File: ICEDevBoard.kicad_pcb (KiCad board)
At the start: 4 copper layers, 100 x 100 mm, 233 parts, among them J101 USB4215-03-A_REVA, J301 program, J401 VGA, J501 Joystick, J502 SJ2-35813B-SMT-TR, J503 Keyboard, J504 Mouse, J505 MSD-1-A, J701 PMOD, Q101 BC847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

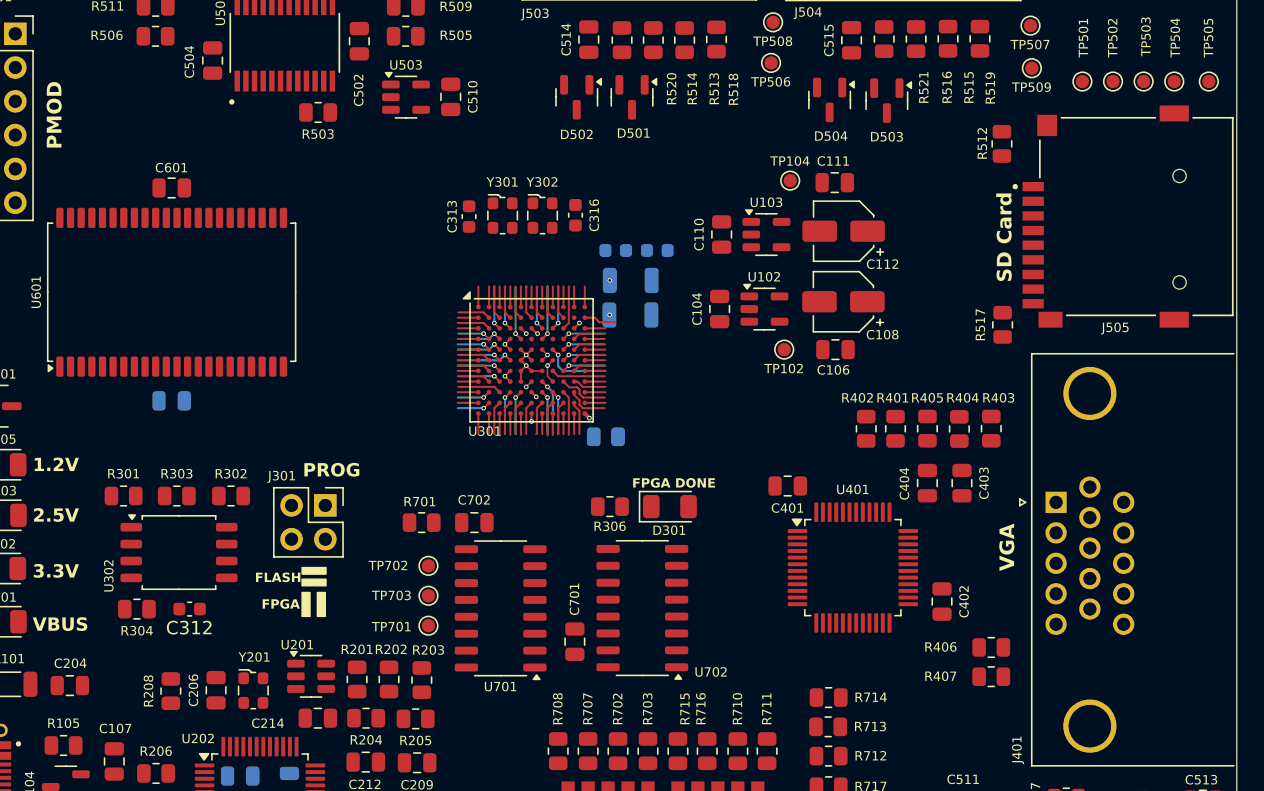
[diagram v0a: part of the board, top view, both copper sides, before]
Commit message: Started board routing
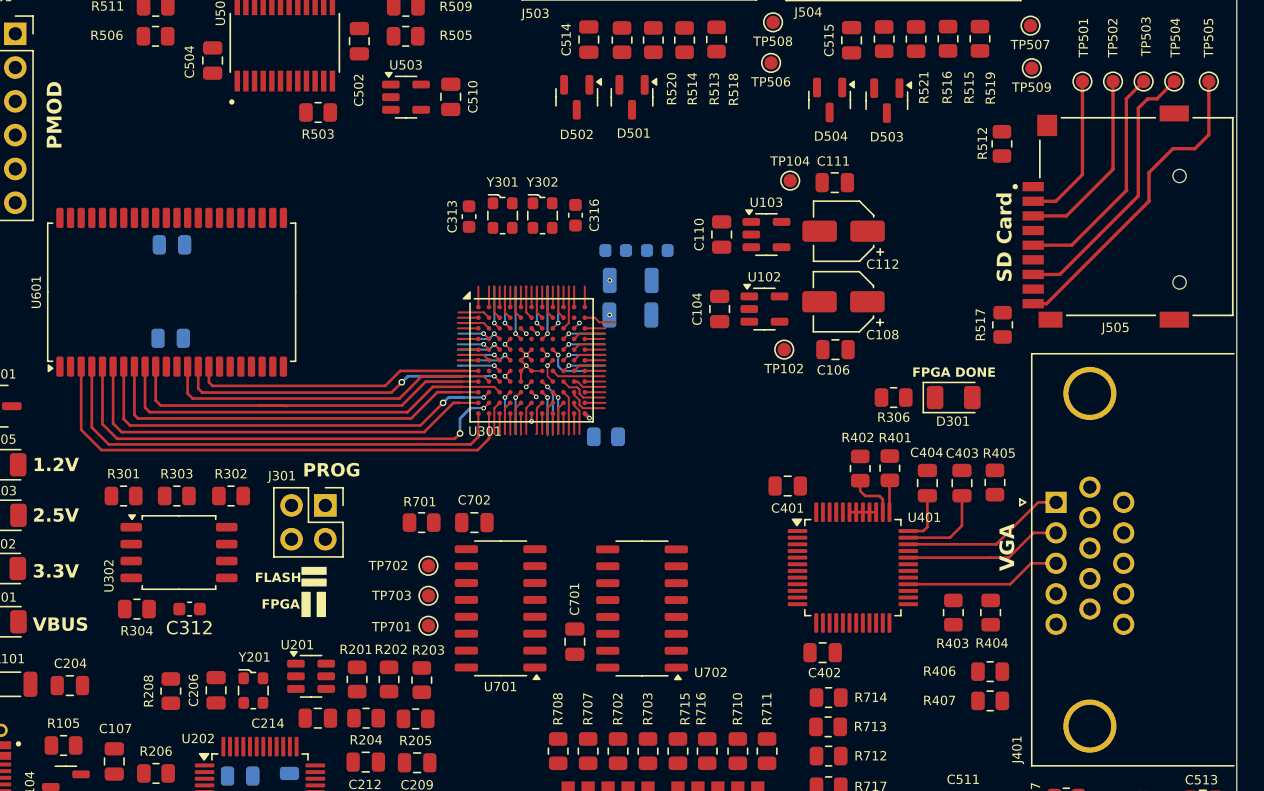
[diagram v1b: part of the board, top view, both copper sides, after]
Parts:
- C601: moved to B.Cu
- moved R306 22.8 mm to (174.2, 93.3)
- moved D301 22.8 mm to (178.7, 93.3)
- moved R403 14.1 mm to (178.7, 109.5), turned to -90 degrees
- moved R404 14.0 mm to (181.5, 109.5), turned to -90 degrees
- moved C402 9.76 mm to (168.9, 112.5), turned to 0 degrees
- moved R405 6.49 mm to (181.8, 99.7)
- moved C602 4.70 mm to (119.9, 88.9)
- moved C601 4.28 mm to (120.0, 81.9)
- moved R402 3.02 mm to (171.7, 98.7), turned to -90 degrees
- moved R401 2.99 mm to (173.9, 98.7), turned to 90 degrees
- moved R406 1.82 mm to (181.5, 114.0)
- moved R407 1.82 mm to (181.5, 116.2)
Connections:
- U301 pad F1: /FPGA/MEM_A7 -> /FPGA/MEM_A6
- U301 pad F2: /FPGA/MEM_A9 -> /FPGA/MEM_A5
- U301 pad G2: /FPGA/MEM_A5 -> /FPGA/MEM_A9
- U301 pad G3: /FPGA/MEM_A6 -> /FPGA/MEM_A7
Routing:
- net /FPGA/MEM_A0: track 1.55 -> 38.5 mm
- net /FPGA/MEM_A1: track 1.55 -> 36.3 mm
- net /FPGA/MEM_A2: track 2.52 -> 35.6 mm, vias 1 -> 2
- net /FPGA/MEM_A3: track 1.55 -> 33.1 mm
- net /FPGA/MEM_A4: track 2.63 -> 33.2 mm, vias 1 -> 2
- net /FPGA/~{SRAM_CE}: track 1.55 -> 30.7 mm
- net /FPGA/MEM_D1: track 1.55 -> 30.0 mm
- net /FPGA/MEM_D0: track 3.27 -> 31.1 mm
- net /FPGA/SD_DETECT: track 3.27 -> 27.0 mm
- net /FPGA/MEM_D2: track 2.52 -> 26.1 mm
- net /FPGA/MEM_D3: track 3.27 -> 25.3 mm, vias 1 -> 2
- net /FPGA/~{SRAM_WE}: track 1.55 -> 22.7 mm
- net /FPGA/SD_MISO: track 2.47 -> 22.9 mm
- net /FPGA/SD_CLOCK: track 1.55 -> 19.0 mm
- net /FPGA/SD_MOSI: track 2.39 -> 16.4 mm
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
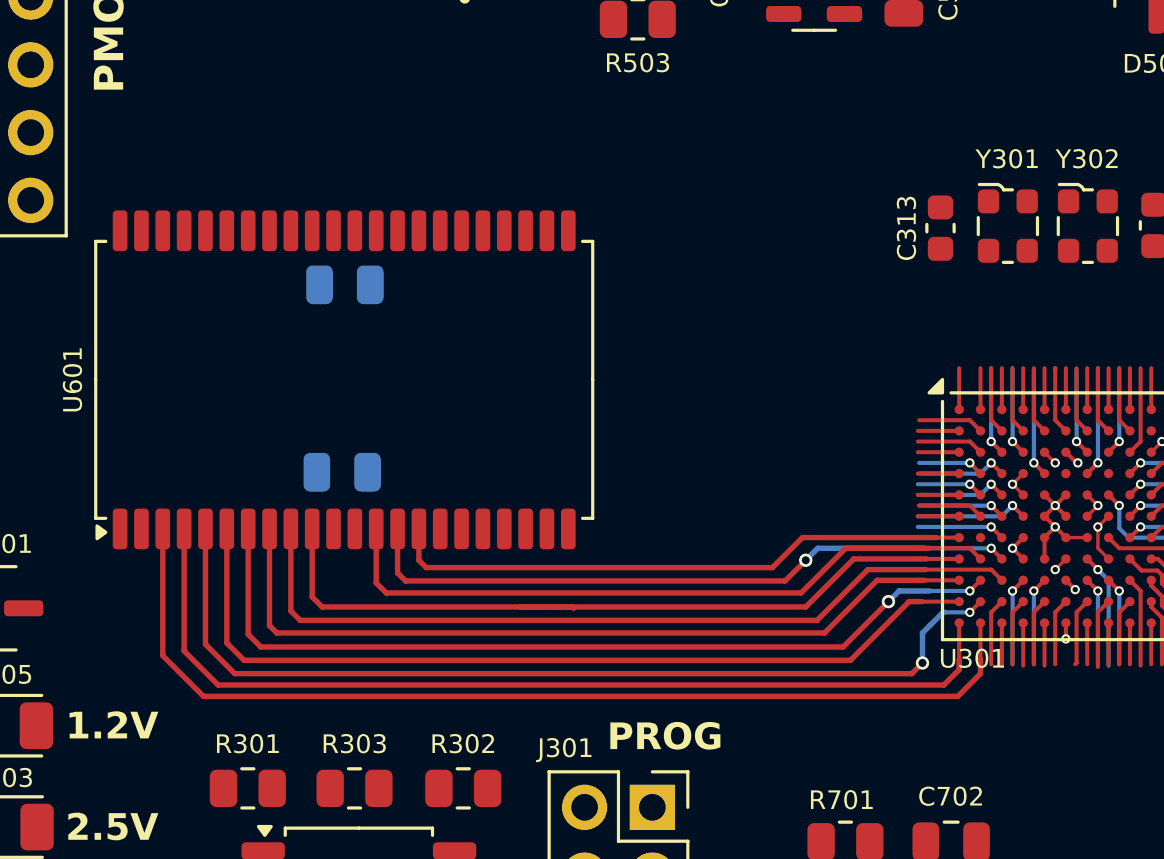
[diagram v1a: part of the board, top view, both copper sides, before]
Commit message: Routed SRAM
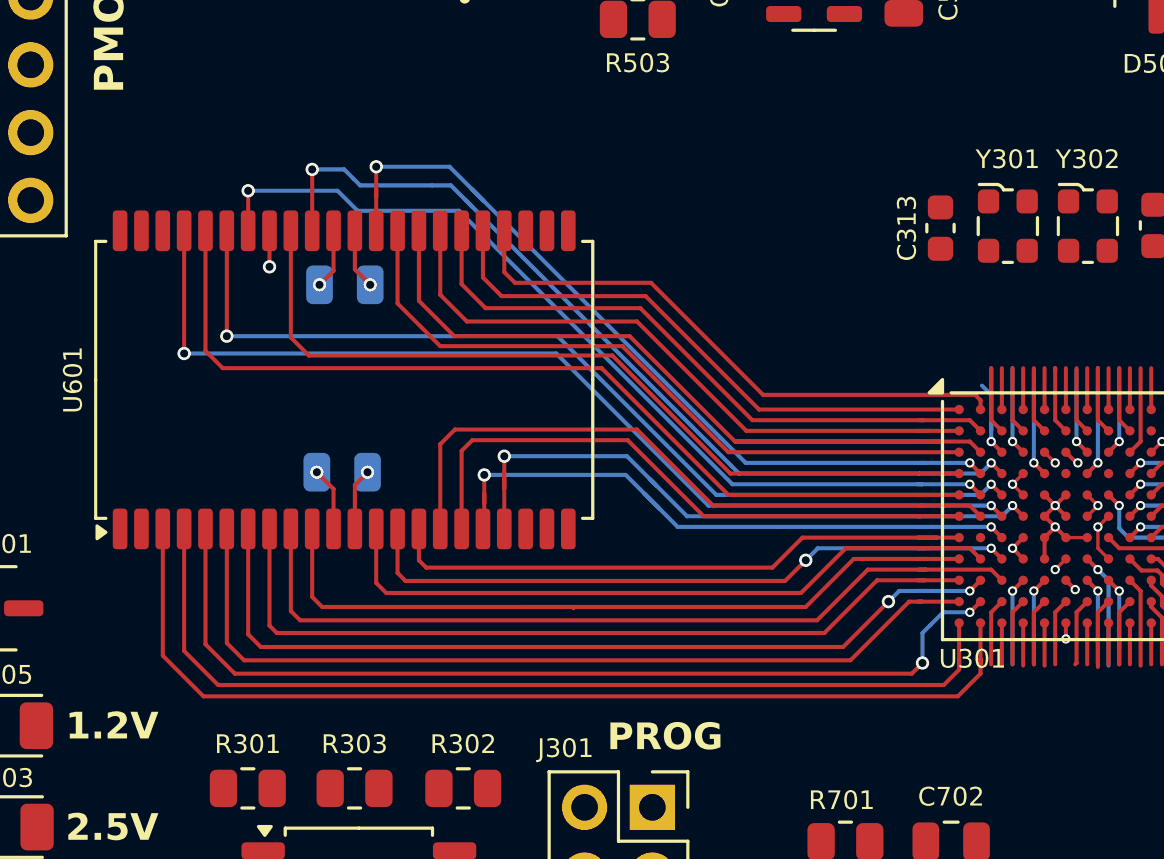
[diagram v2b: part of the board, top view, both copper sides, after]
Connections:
- U301 pad A1: /FPGA/MEM_A10 -> /FPGA/MEM_A11
- U301 pad A2: /FPGA/MEM_A11 -> /FPGA/MEM_A10
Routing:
- net /FPGA/MEM_A18: track 3.27 -> 37.8 mm, vias 1 -> 2
- net /FPGA/MEM_A17: track 1.55 -> 35.1 mm
- net /FPGA/MEM_A16: track 3.48 -> 35.8 mm, vias 1 -> 2
- net /FPGA/MEM_A15: track 2.52 -> 33.8 mm, vias 1 -> 2
- net /FPGA/MEM_A14: track 2.52 -> 33.7 mm
- net /FPGA/MEM_D6: track 3.53 -> 33.7 mm, vias 1 -> 2
- net /FPGA/MEM_D7: track 1.55 -> 31.2 mm
- net /FPGA/MEM_D5: track 2.47 -> 31.0 mm, vias 1 -> 2
- net /FPGA/MEM_D4: track 1.55 -> 26.1 mm
- net /FPGA/MEM_A13: track 1.55 -> 24.4 mm
- net /FPGA/MEM_A5: track 2.47 -> 25.1 mm
- net /FPGA/MEM_A6: track 1.55 -> 23.1 mm
- net /FPGA/MEM_A12: track 2.47 -> 23.9 mm
- net /FPGA/MEM_A8: track 4.28 -> 24.5 mm, vias 1 -> 2
- net /FPGA/MEM_A10: track 1.55 -> 21.7 mm
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
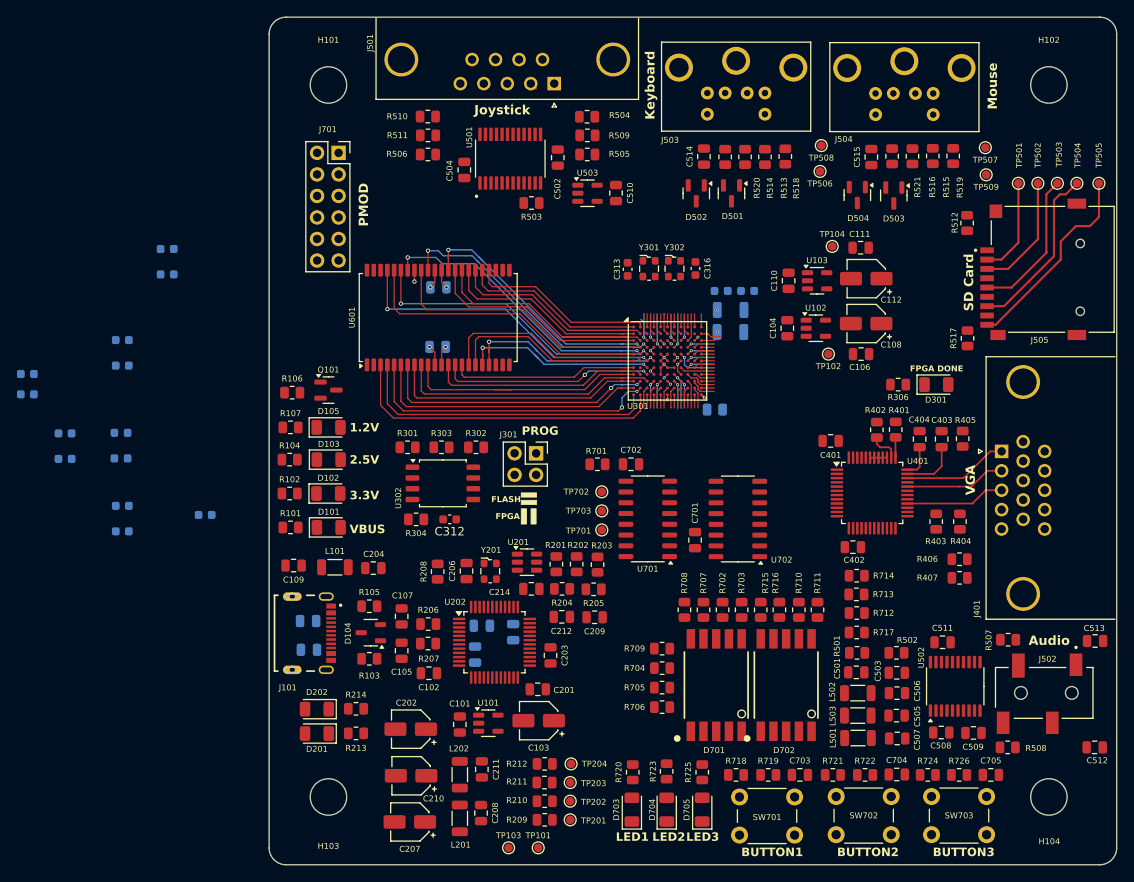
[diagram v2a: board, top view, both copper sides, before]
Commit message: Additional routing
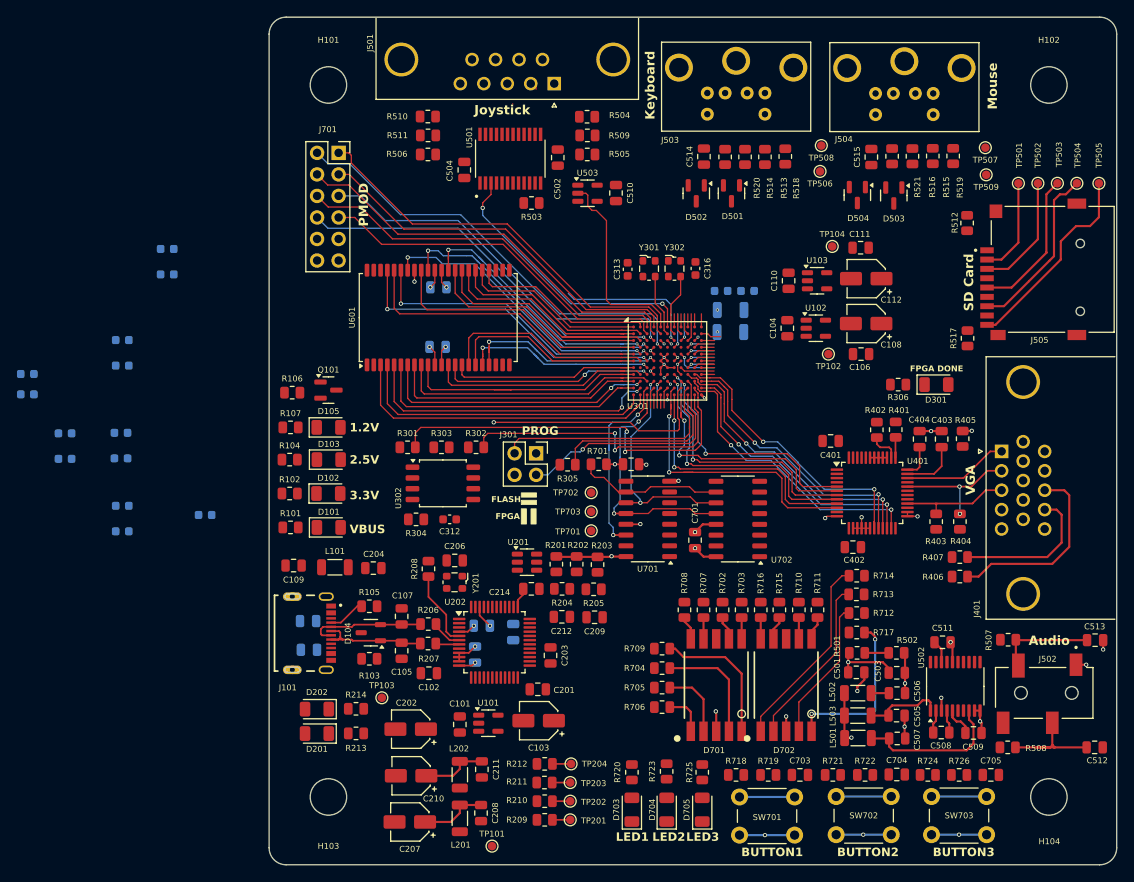
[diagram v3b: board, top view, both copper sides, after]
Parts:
- R305: moved to F.Cu
- moved TP103 23.2 mm to (113.3, 130.3)
- moved R305 18.6 mm to (135.2, 102.8), turned to 180 degrees
- moved TP101 5.45 mm to (126.3, 147.8)
- moved Y201 4.41 mm to (121.9, 116.7), turned to -90 degrees
- moved R407 2.45 mm to (181.5, 113.7), turned to 180 degrees
- moved R406 2.05 mm to (181.5, 116.0), turned to 180 degrees
- moved C206 1.87 mm to (121.9, 114.1), turned to 180 degrees
- moved TP701 1.25 mm to (138.0, 110.6)
- moved TP702 1.25 mm to (138.0, 106.1)
- moved TP703 1.25 mm to (138.0, 108.3)
- moved R208 1.14 mm to (118.8, 115.1)
- moved R701 0.15 mm to (138.9, 102.8)
- moved C513 0.10 mm to (197.4, 123.5), turned to 0 degrees
- moved R720 0.10 mm to (142.8, 139.1), turned to -90 degrees
- turned R715 to -90 degrees
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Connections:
- U301 pad H7: /FPGA/VGA_G3 -> /FPGA/VGA_G2
- U301 pad J7: /FPGA/VGA_G1 -> /FPGA/VGA_G3
- U301 pad J8: /FPGA/VGA_G5 -> /FPGA/VGA_G0
- U301 pad K7: /FPGA/VGA_G0 -> /FPGA/VGA_G5
- U301 pad L7: /FPGA/VGA_G2 -> /FPGA/VGA_G4
- U301 pad L8: /FPGA/VGA_G4 -> /FPGA/VGA_G1
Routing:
- net GND: track 15.8 -> 74.2 mm, vias 8 -> 29
- net /FPGA/PMOD4: track 4.07 -> 51.7 mm
- net /FPGA/PMOD0: track 2.52 -> 48.4 mm
- net /FPGA/PMOD5: track 2.52 -> 48.4 mm
- net /FPGA/~{FTDI_SPISS}: track 2.52 -> 48.3 mm, vias 0 -> 2
- net /FPGA/PMOD6: track 1.55 -> 45.8 mm
- net /FPGA/PMOD1: track 1.55 -> 45.4 mm
- net /FPGA/PMOD2: track 3.32 -> 45.4 mm
- net /FPGA/PMOD3: track 2.52 -> 42.6 mm
- net /FPGA/PMOD7: track 5.16 -> 45.0 mm
- net +3V3: track 9.90 -> 48.7 mm, vias 7 -> 17
- net /FPGA/FTDI_SPICLK: track 1.55 -> 36.9 mm, vias 0 -> 2
- net /FPGA/VGA_G5: track 3.32 -> 35.0 mm, vias 1 -> 2
- net /FPGA/VGA_B4: track 3.12 -> 34.6 mm, vias 0 -> 2
- net /FPGA/JOY_D0: track 1.55 -> 32.7 mm, vias 0 -> 2
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
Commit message: More layout done
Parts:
- moved R306 71.8 mm to (102.4, 94.9)
- moved D301 71.8 mm to (107.0, 94.9)
- moved Q101 3.95 mm to (107.1, 90.0)
- moved R106 3.95 mm to (102.9, 90.3)
- moved C701 1.30 mm to (151.6, 111.8)
- moved U702 1.18 mm to (156.5, 109.2)
- moved C109 0.35 mm to (102.6, 114.9)
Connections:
- U301 pad A10: /FPGA/MOUSE_DATA -> /FPGA/MOUSE_CLK
- U301 pad A7: /FPGA/JOY_D1 -> /FPGA/JOY_D5
- U301 pad C7: /FPGA/JOY_D5 -> /FPGA/JOY_D2
- U301 pad C9: /FPGA/MOUSE_CLK -> /FPGA/MOUSE_DATA
- U301 pad D7: /FPGA/JOY_D2 -> /FPGA/JOY_D1
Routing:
- net /FPGA/SND_BCK: track 1.50 -> 89.9 mm
- net /FPGA/SND_DIN: track 3.27 -> 90.7 mm, vias 1 -> 2
- net /FPGA/SND_LRCK: track 2.47 -> 89.6 mm
- net /FPGA/VGA_HSYNC: track 2.47 -> 61.6 mm, vias 0 -> 2
- net /FPGA/VGA_VSYNC: track 3.32 -> 55.5 mm, vias 1 -> 4
- net /FPGA/SD_MISO: track 22.9 -> 59.7 mm
- net /FPGA/SD_DETECT: track 27.0 -> 63.4 mm, vias 1 -> 2
- net /FPGA/SD_SELECT: track 13.1 -> 48.5 mm
- net /FPGA/JOY_D1: track 1.55 -> 36.6 mm, vias 0 -> 2
- net /FPGA/VGA_CLOCK: track 1.55 -> 36.5 mm, vias 0 -> 2
- net /FPGA/SD_MOSI: track 16.4 -> 51.2 mm
- net /FPGA/SD_CLOCK: track 19.0 -> 53.7 mm
- net /FPGA/~{VGA_BLANK}: track 1.55 -> 36.1 mm, vias 0 -> 2
- net /FPGA/JOY_D3: track 2.52 -> 35.5 mm, vias 0 -> 2
- net /FPGA/JOY_D2: track 4.12 -> 34.4 mm, vias 1 -> 2
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
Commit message: More layout changes
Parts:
- C402: moved to B.Cu
- moved TP103 16.9 mm to (115.3, 113.5)
- moved R503 9.38 mm to (136.4, 64.3)
- moved C204 5.65 mm to (106.7, 114.9)
- moved C502 5.53 mm to (132.2, 71.8), turned to 180 degrees
- moved C510 5.12 mm to (146.0, 71.2)
- moved U503 5.12 mm to (142.7, 71.2)
- moved R509 4.79 mm to (136.4, 68.6), turned to 180 degrees
- moved L101 3.46 mm to (111.2, 114.9)
- moved R511 2.45 mm to (118.8, 61.5)
- moved R510 2.18 mm to (118.8, 63.9)
- moved R512 1.32 mm to (182.1, 75.6), turned to -90 degrees
- moved R505 1.16 mm to (136.4, 66.5), turned to 180 degrees
- moved R504 1.15 mm to (136.4, 62.1)
- moved C402 0.74 mm to (169.6, 112.4)
- moved R517 0.67 mm to (182.4, 87.2)
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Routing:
- net +5V: track 0.00 -> 226.5 mm, vias 0 -> 14
- net GND: track 83.1 -> 176.3 mm, vias 34 -> 95
- net /FPGA/BUTTON3: track 2.52 -> 89.2 mm, vias 0 -> 2
- net /FPGA/BUTTON2: track 1.62 -> 77.4 mm, vias 0 -> 2
- net +3V3: track 54.5 -> 114.7 mm, vias 22 -> 63
- net /FPGA/BUTTON1: track 2.52 -> 62.0 mm, vias 0 -> 2
- net /FPGA/LED1: track 1.60 -> 60.0 mm, vias 0 -> 2
- net /FPGA/LED3: track 3.39 -> 58.4 mm, vias 1 -> 2
- net /FPGA/LED2: track 2.52 -> 55.7 mm, vias 0 -> 2
- net VBUS: track 0.00 -> 47.5 mm
- net /Peripherals/JOY_SEL5V: track 0.00 -> 29.3 mm
- net /FPGA/CDONE: track 27.5 -> 56.2 mm, vias 1 -> 2
- net Net-(U702-QH): track 0.00 -> 27.7 mm
- net Net-(U202-ADBUS0): track 0.00 -> 23.4 mm, vias 0 -> 2
- net Net-(J504-Pad2): track 0.00 -> 23.2 mm, vias 0 -> 2
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
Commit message: Reworking layout
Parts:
- C203: moved to B.Cu
- moved TP101 66.3 mm to (103.9, 85.4)
- moved D201 28.7 mm to (131.6, 146.7)
- moved D202 25.7 mm to (126.5, 146.7)
- moved C202 22.4 mm to (104.2, 115.5)
- moved C204 20.9 mm to (126.8, 120.6), turned to 90 degrees
- moved U101 20.4 mm to (116.9, 115.0)
- moved C101 20.4 mm to (113.5, 115.1)
- moved C103 20.4 mm to (122.8, 114.7)
- moved R213 18.8 mm to (127.6, 141.9), turned to 90 degrees
- moved R214 18.1 mm to (125.1, 141.9), turned to 90 degrees
- moved C102 15.9 mm to (128.4, 114.7), turned to 0 degrees
- moved C211 11.2 mm to (114.2, 136.3), turned to 0 degrees
- moved C208 9.38 mm to (119.3, 136.4), turned to 0 degrees
- moved TP103 7.77 mm to (114.8, 121.2)
- moved L202 7.74 mm to (114.8, 138.9), turned to 180 degrees
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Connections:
- C202 pad 1: VBUS -> +5V
- C204 pad 1: VBUS -> +5V
- U202 pad 40: VBUS -> +5V
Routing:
- net +5V: track 226.5 -> 199.7 mm, vias 14 -> 13
- net Net-(U201-CLK): track 5.82 -> 20.1 mm, vias 0 -> 2
- net /USB Programming/~{RX_LED}: track 20.4 -> 6.73 mm
- net Net-(U202-~{RESET}): track 4.70 -> 14.6 mm
- net VBUS: track 47.5 -> 37.7 mm, vias 0 -> 2
- net Net-(U201-DI): track 5.74 -> 15.4 mm
- net Net-(U202-ADBUS0): track 23.4 -> 14.9 mm, vias 2 -> 0
- net Net-(U202-ADBUS2): track 17.9 -> 9.88 mm, vias 2 -> 0
- net Net-(U202-ADBUS1): track 20.5 -> 13.5 mm, vias 2 -> 0
- net Net-(U202-ADBUS4): track 15.1 -> 8.03 mm, vias 2 -> 0
- net /USB Programming/~{TX_LED}: track 22.0 -> 15.1 mm
- net Net-(D201-K): track 2.31 -> 8.22 mm
- net Net-(U202-XCSI): track 0.00 -> 4.76 mm
- net +3V3: track 114.7 -> 110.1 mm, vias 63 -> 64
- net Net-(D202-K): track 2.32 -> 5.53 mm
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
